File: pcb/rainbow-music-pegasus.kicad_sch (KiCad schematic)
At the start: 106 parts, among them J1 USB_B_Micro, J2 Conn_02x03_Odd_Even, J3 B2B-PH-K-S, Q1 DMG3415U, SW1 SW_SPDT, SW2 EVQQ2, U1 ESP32-C3-MINI-1, U2 OPA344NA, U3 TLV75533PDBV, U4 MCP73831-2-OT

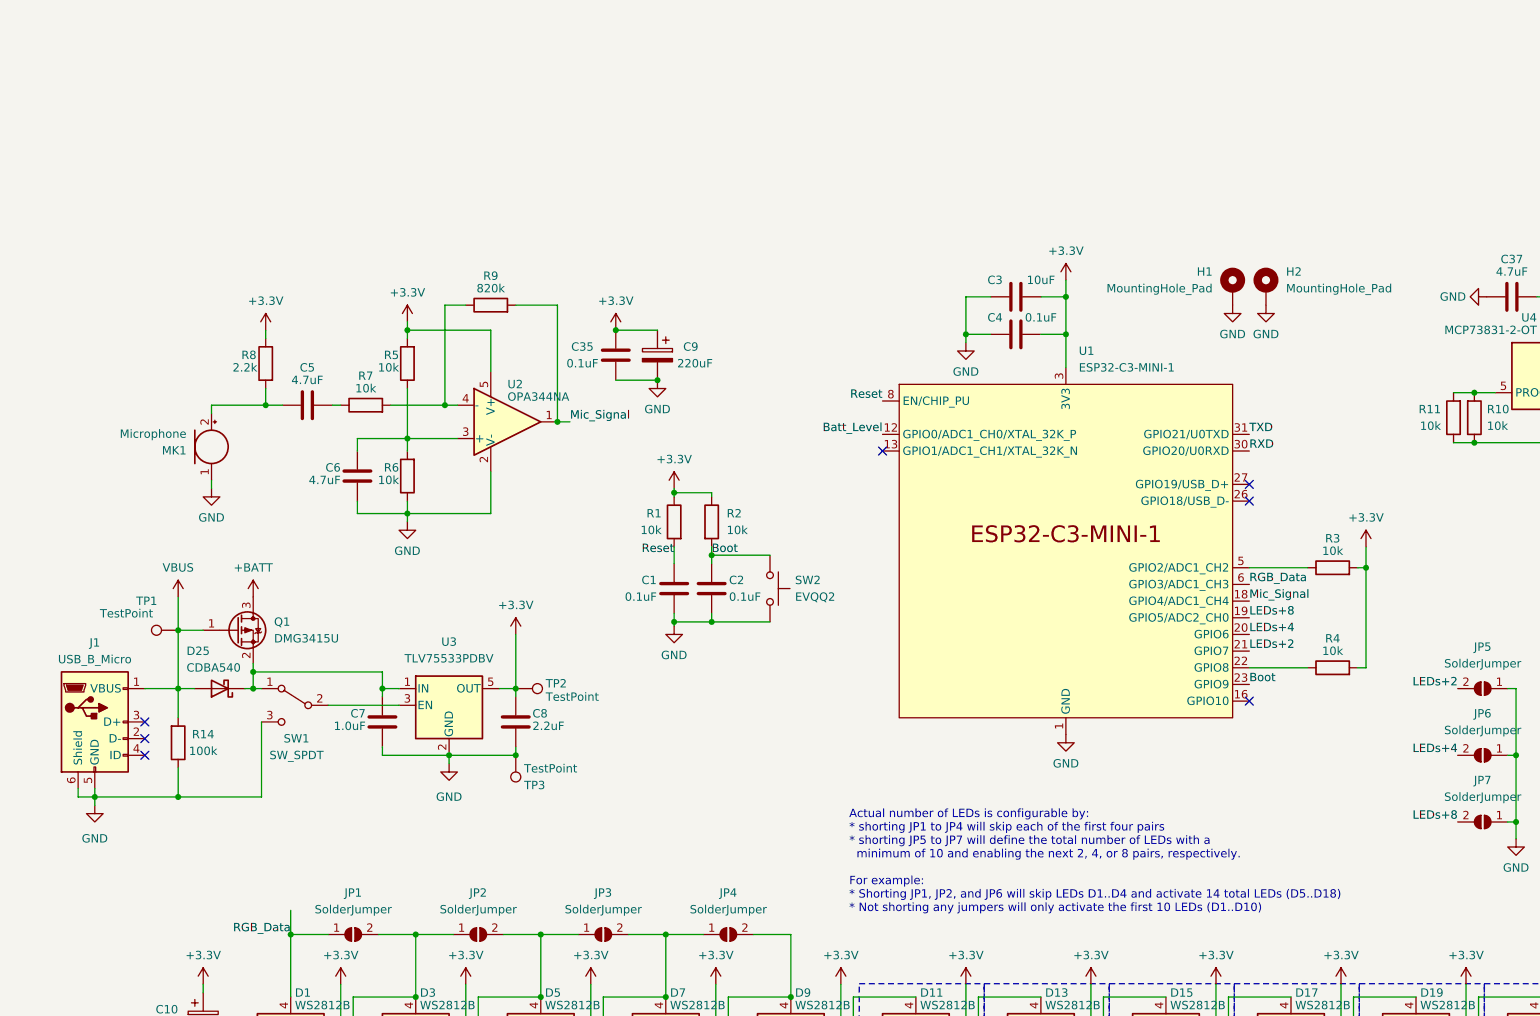
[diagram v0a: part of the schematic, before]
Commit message: Add on a digital potentiometer and a dual-channel amp to dynamically capture quiet or loud music
Includes major realignment of entire top-left corner, chip changes,
rerouting traces, etc.
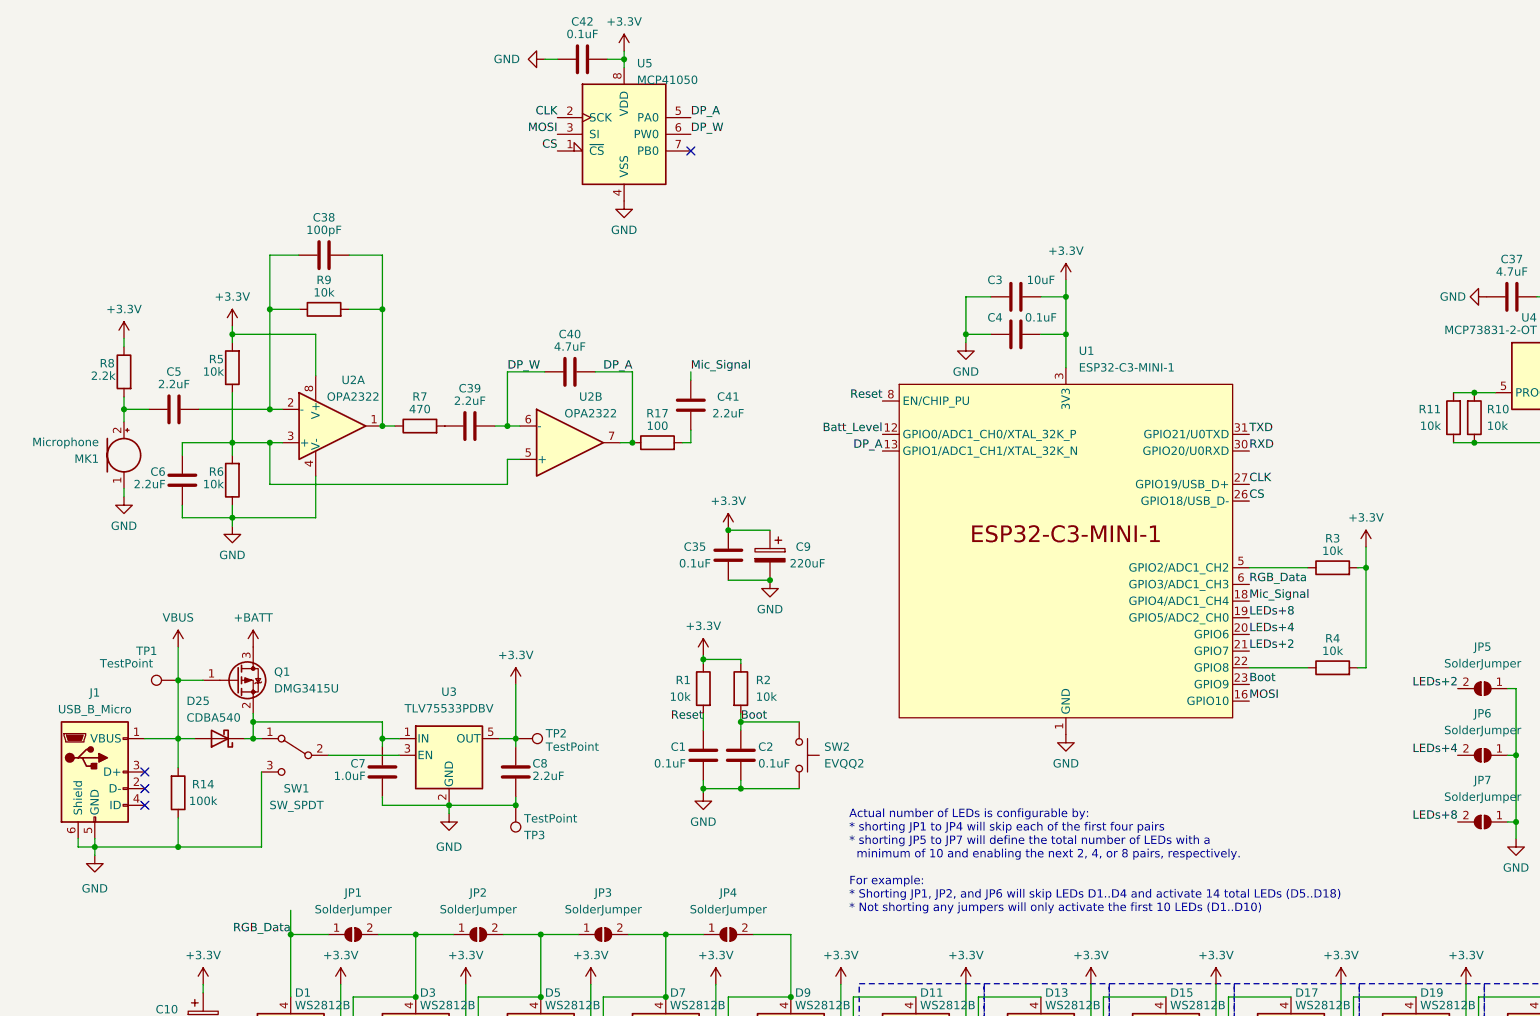
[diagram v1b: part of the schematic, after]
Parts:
- removed H1, H2: MountingHole_Pad, MountingHole:MountingHole_2.2mm_M2_Pad_Via, symbol Mechanical:MountingHole_Pad
- removed U2: OPA344NA, Package_TO_SOT_SMD:SOT-23-5, symbol Amplifier_Operational:OPA340NA
- added C38: 100pF, Capacitor_SMD:C_0805_2012Metric, symbol Device:C
- added C39, C41: 2.2uF, Capacitor_SMD:C_0805_2012Metric, symbol Device:C
- added C40: 4.7uF, Capacitor_SMD:C_0805_2012Metric, symbol Device:C
- added C42: 0.1uF, Capacitor_SMD:C_0603_1608Metric, symbol Device:C
- added R17: 100, Resistor_SMD:R_0805_2012Metric, symbol Device:R
- added U2: OPA2322, Package_SO:SOIC-8_3.9x4.9mm_P1.27mm, symbol Amplifier_Operational:OPA2325
- added U5: MCP41050, Package_SO:SOIC-8_3.9x4.9mm_P1.27mm, symbol Potentiometer_Digital:MCP41050
- C5, C6: value 4.7uF -> 2.2uF
- R7: value 10k -> 470
- R9: value 820k -> 10k
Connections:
- net +3.3V: now also C42.1, U2.8 (V+), U5.8 (VDD)
- net GND: now also C42.2, U2.4 (V-), U5.4 (VSS)
- net Mic_Signal: now also C41.1; no longer R9.2
- net at C5.2: now also R9.1, C38.1, U2.2 (-); no longer R7.1
- net at R7.2: now also C39.1; no longer R9.1
- net at C6.2, R5.1, R6.2: now also U2.3 (+), U2.5 (+)
- net DP_A: now reaches U1.13 (GPIO1/ADC1_CH1/XTAL_32K_N)
- net DP_A: now also C40.2, R17.1, U2.7, U5.5 (PA0)
- net MOSI: now reaches U1.16 (GPIO10)
- net MOSI: now also U5.3 (SI)
- net CS: now reaches U1.26 (GPIO18/USB_D-)
- net CS: now also U5.1 (~{CS})
- net CLK: now reaches U1.27 (GPIO19/USB_D+)
- net CLK: now also U5.2 (SCK)
- new net: C38.2, R7.1, R9.2, U2.1
- new net: C41.2, R17.2
- new net DP_W: C39.2, C40.1, U2.6 (-), U5.6 (PW0)
- no-connect marks 9 -> 6
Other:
- moved on the sheet: C1, C2, C35, C5, C6, C7, C8, C9, D25, J1, MK1, Q1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

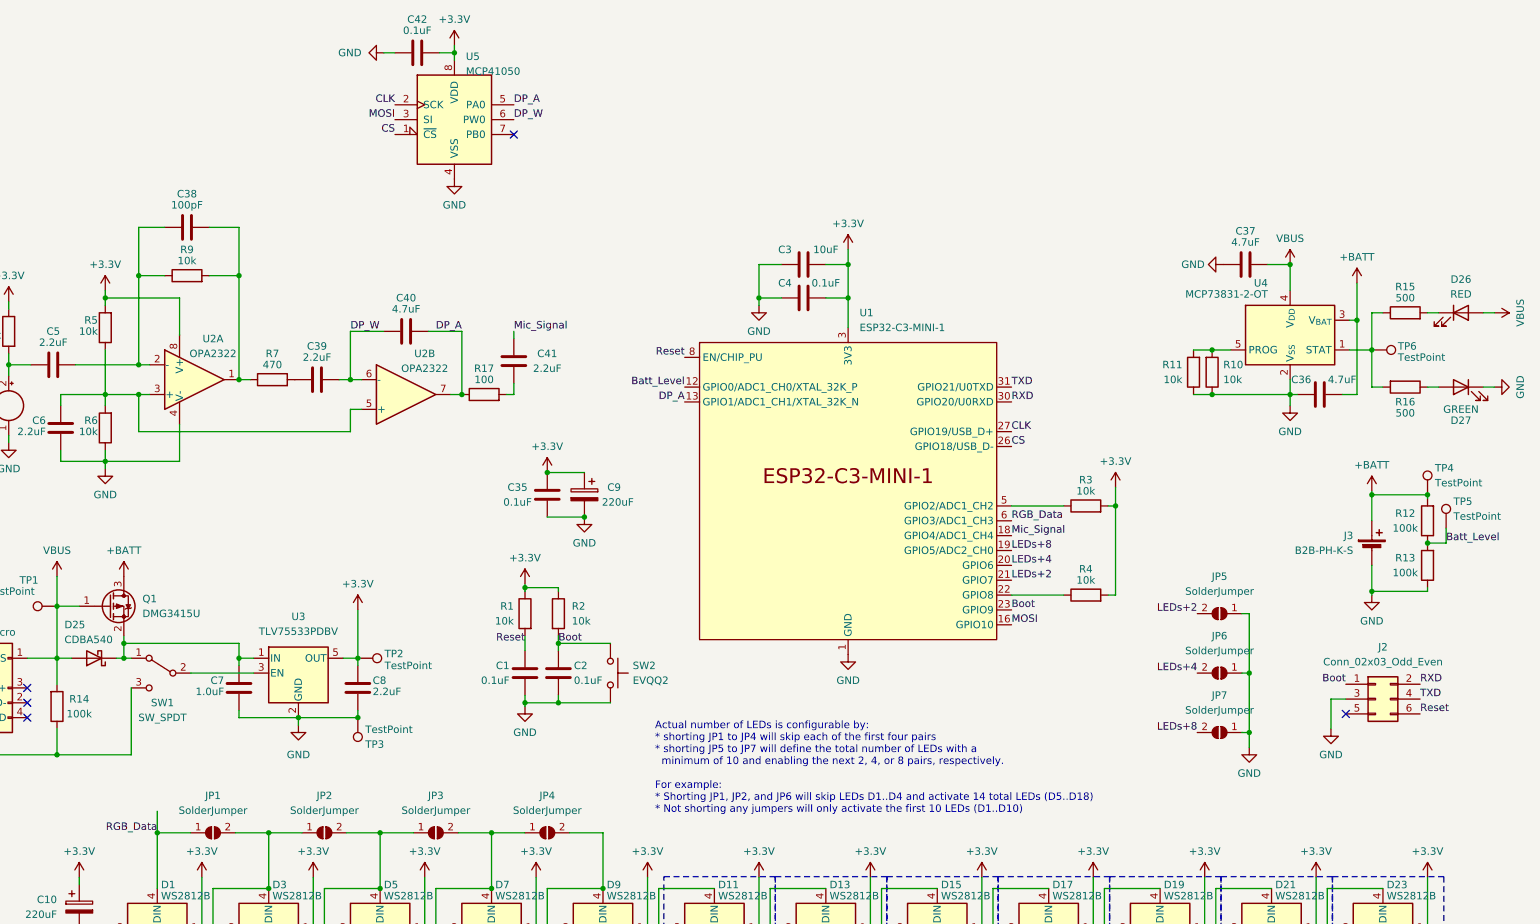
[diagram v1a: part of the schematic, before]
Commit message: Updated gerbers, schematics, BOM to match recent pcb layout updates
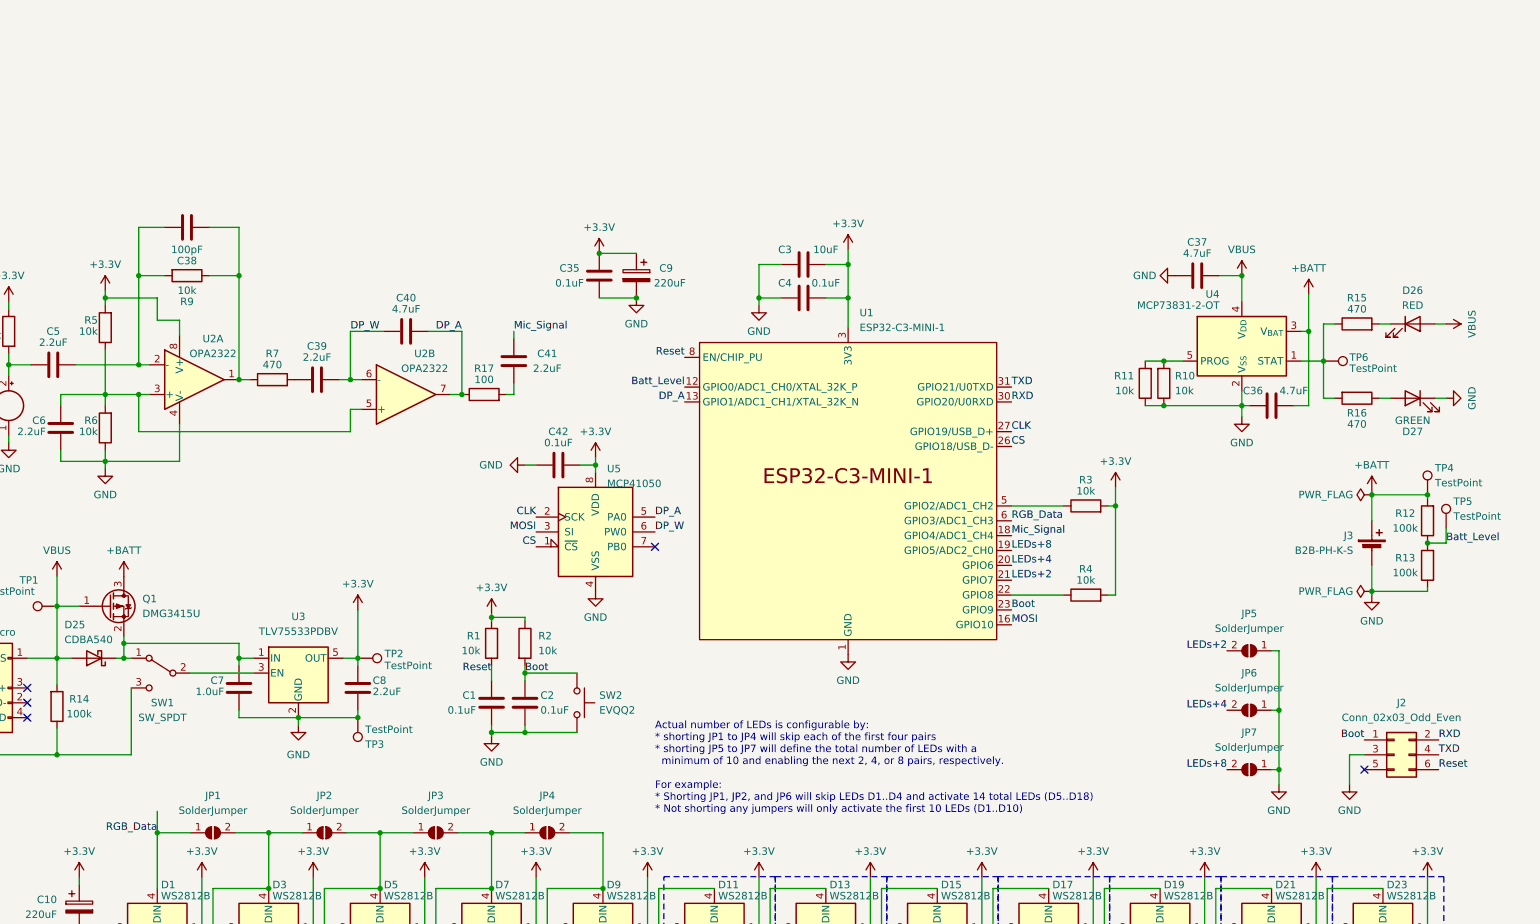
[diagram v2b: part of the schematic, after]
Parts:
- J2, JP1, JP2, JP3, JP4, JP5, JP6, JP7, TP1, TP2, TP3, TP4, TP5, TP6: now left out of the parts list
- R15, R16: value 500 -> 470
- R7: footprint Resistor_SMD:R_0805_2012Metric -> Resistor_SMD:R_0603_1608Metric
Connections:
- net at C38.1, C5.2, U2.2 (-): now also R9.2; no longer R9.1
- net at C38.2, R7.1, U2.1: now also R9.1; no longer R9.2
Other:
- moved on the sheet: C1, C2, C35, C36, C37, C42, C9, D26, D27, J2, JP5, JP6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

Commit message: Update design to KiCad 9
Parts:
- U2: Order (none) -> https://www.digikey.ca/en/products/detail/texas-instruments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
- U5: Order (none) -> https://www.digikey.ca/en/products/detail/microchip-technol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
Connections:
- net DP_W: now also C40.2, R17.1, U2.7, U5.5 (PA0); no longer C39.2, C40.1, U2.6 (-)
- net GND: now also JP5.2 (B), JP6.2 (B), JP7.2 (B); no longer JP5.1 (A), JP6.1 (A), JP7.1 (A)
- net LEDs+2: now also JP5.1 (A); no longer JP5.2 (B)
- net LEDs+4: now also JP6.1 (A); no longer JP6.2 (B)
- net LEDs+8: now also JP7.1 (A); no longer JP7.2 (B)
- net DP_B: now reaches U5.7 (PB0)
- net DP_B: now also C39.2, C40.1, U2.6 (-)
- removed net DP_A: C40.2, R17.1, U1.13 (GPIO1/ADC1_CH1/XTAL_32K_N), U2.7, U5.5 (PA0)
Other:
- note added: "Actual number of LEDs is configurable by: * shorting JP1 to JP4 to skip each of the first four pairs * shorting JP5 to JP7 to define the total number of LEDs with a minimum of 10 and enabling the next 2, 4, or 8 pairs, respectively. For example: * Shorting JP1, JP2, and JP6 will skip LEDs D1..D4 and activate 14 total LEDs (D5..D18) * Not shorting any jumpers will only activate the first 10 LEDs (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"
- note added: "Audio"
- note added: "Display"
- note added: "MCU"
- note added: "Power"
- note removed: "Actual number of LEDs is configurable by: * shorting JP1 to JP4 will skip each of the first four pairs * shorting JP5 to JP7 will define the total number of LEDs with a minimum of 10 and enabling the next 2, 4, or 8 pairs, respectively. For example: * Shorting JP1, JP2, and JP6 will skip LEDs D1..D4 and activate 14 total LEDs (D5..D18) * Not shorting any jumpers will only activate the first 10 LE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"
- moved on the sheet: C1, C10, C11, C12, C13, C14, C15, C16, C17, C18, C19, C2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
